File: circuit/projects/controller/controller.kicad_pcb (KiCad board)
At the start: 2 copper layers, 95 x 145 mm, 50 parts, among them J1 Conn_01x02, SW1 SW_DIP_x01, SW10 SW_DIP_x01, SW2 SW_DIP_x01, SW3 SW_DIP_x01, SW4 SW_DIP_x01, SW5 SW_DIP_x01, SW6 SW_DIP_x01, SW7 SW_DIP_x01, SW8 TOGGLE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

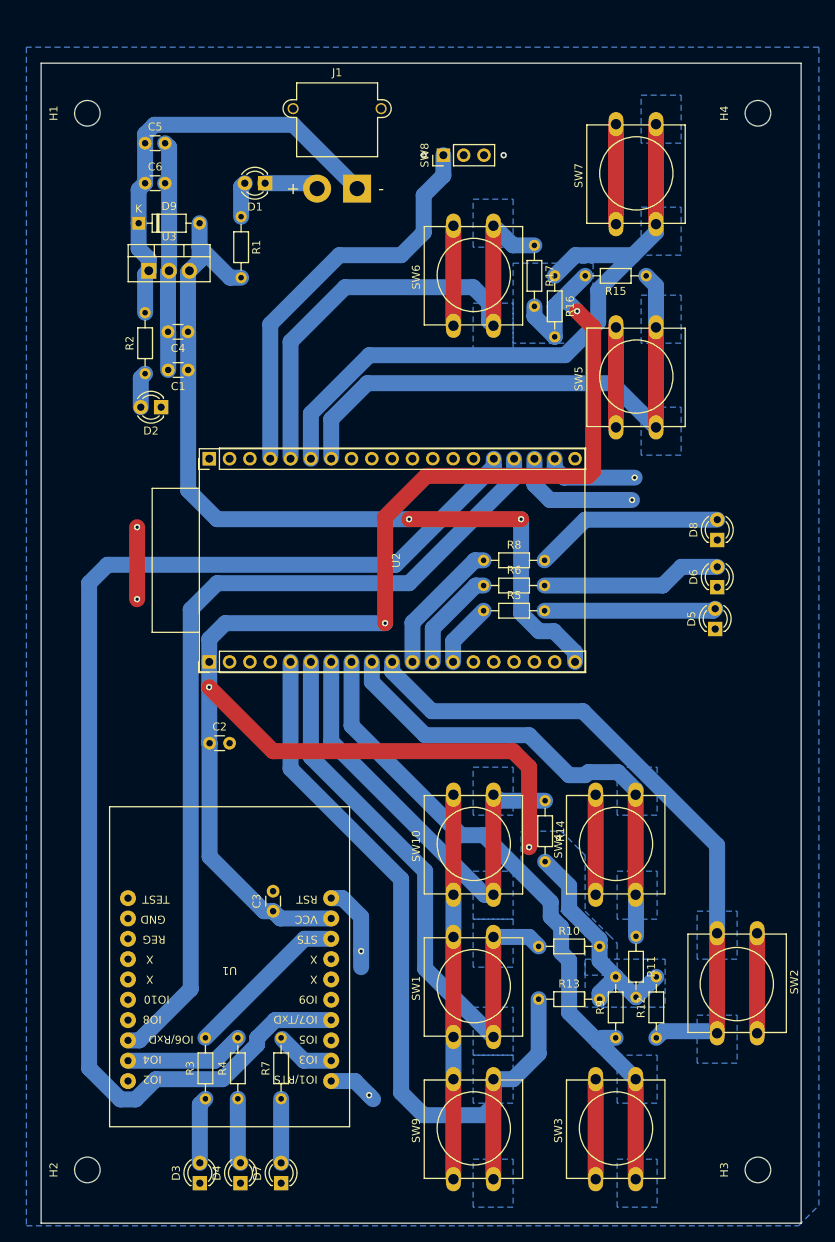
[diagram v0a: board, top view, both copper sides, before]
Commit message: ESPのフットプリント違ったので修正します
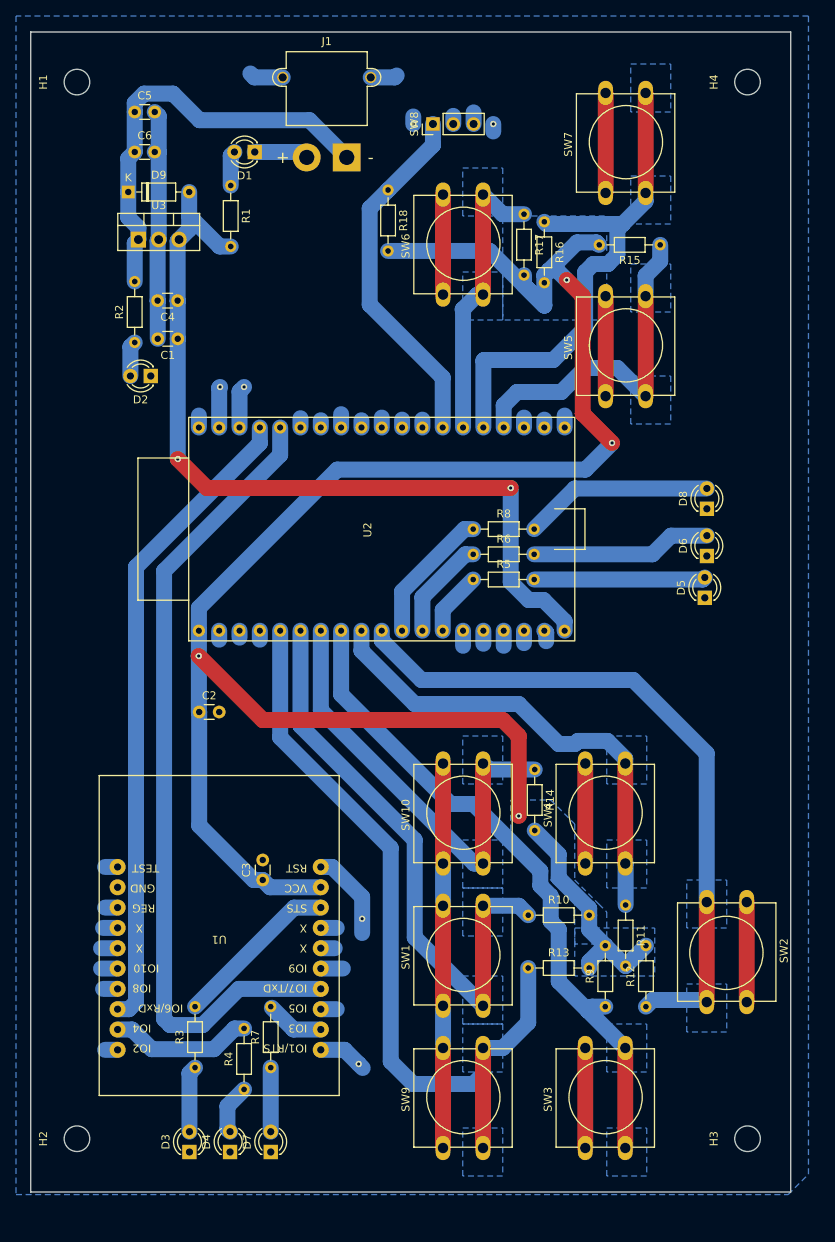
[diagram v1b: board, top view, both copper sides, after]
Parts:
- added R18: 10k, Resistor_THT:R_Axial_DIN0204_L3.6mm_D1.6mm_P7.62mm_Horizontal, F.Cu at (148.1, 41.9)
- U2: footprint Boad_dev:ESP32-DevKitC -> ESP32_fot:ESP32
- moved R16 6.88 mm to (167.6, 45.8)
- moved R15 4.25 mm to (182.1, 48.7)
- moved C3 4.11 mm to (132.4, 128.1)
- moved D2 4.11 mm to (118.4, 65.1)
- moved D5 4.11 mm to (187.6, 92.8)
- moved D7 4.11 mm to (133.4, 162.1)
- moved H3 4.11 mm to (193.0, 160.4)
- moved R10 4.11 mm to (165.6, 132.5)
- moved R12 4.11 mm to (180.3, 143.9)
- moved R13 4.11 mm to (165.6, 139.1)
- moved R17 4.11 mm to (165.0, 44.9)
- moved R2 4.11 mm to (116.4, 60.9)
- moved R6 4.11 mm to (158.7, 87.4)
- moved R8 4.11 mm to (158.7, 84.2)
- moved R9 4.11 mm to (175.2, 143.9)
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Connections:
- J1 pad : (no net) -> GND
- U2 pad 23: sw8 -> sw5
- U2 pad 24: sw6 -> sw7
- U2 pad 25: sw7 -> sw6
- U2 pad 26: sw5 -> sw8
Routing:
- net IM920TX: track 154.7 -> 101.7 mm
- net sw6: track 64.6 -> 36.7 mm
- net IM920RX: track 107.6 -> 80.9 mm
- net sw5: track 69.0 -> 43.6 mm
- net +3.3V: track 230.7 -> 253.9 mm
- net sw7: track 84.9 -> 66.3 mm
- net BUSY: track 22.4 -> 11.5 mm
- net RESET: track 22.7 -> 16.3 mm
- net sw8: track 51.3 -> 45.0 mm
- net sw2: track 82.4 -> 86.8 mm
- net GND: track 168.0 -> 171.9 mm, vias 2 -> 0
- net SLEEP: track 14.9 -> 17.9 mm
- net unconnected-(U1-IO9-Pad9): track 0.00 -> 2.76 mm
- net unconnected-(U1-NC-Pad12): track 0.00 -> 2.07 mm
- net unconnected-(U1-IO10-Pad10): track 0.00 -> 2.07 mm
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- added copper zone on B.Cu, net sw10
- removed copper zone on B.Cu, net sw8
